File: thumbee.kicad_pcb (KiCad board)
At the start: 2 copper layers, 1 part, among them U1 msc313e

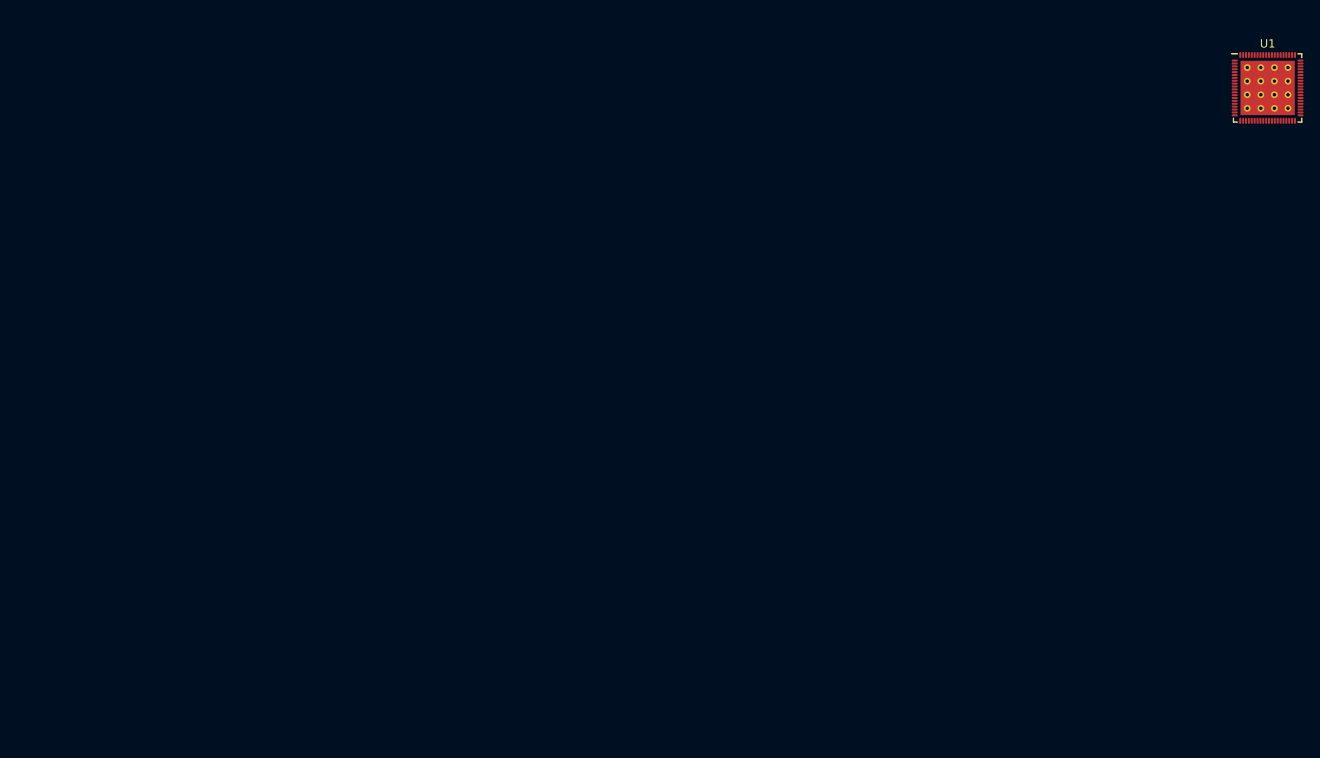
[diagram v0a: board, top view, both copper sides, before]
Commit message: Fix schematic bugs. Assign footprints.
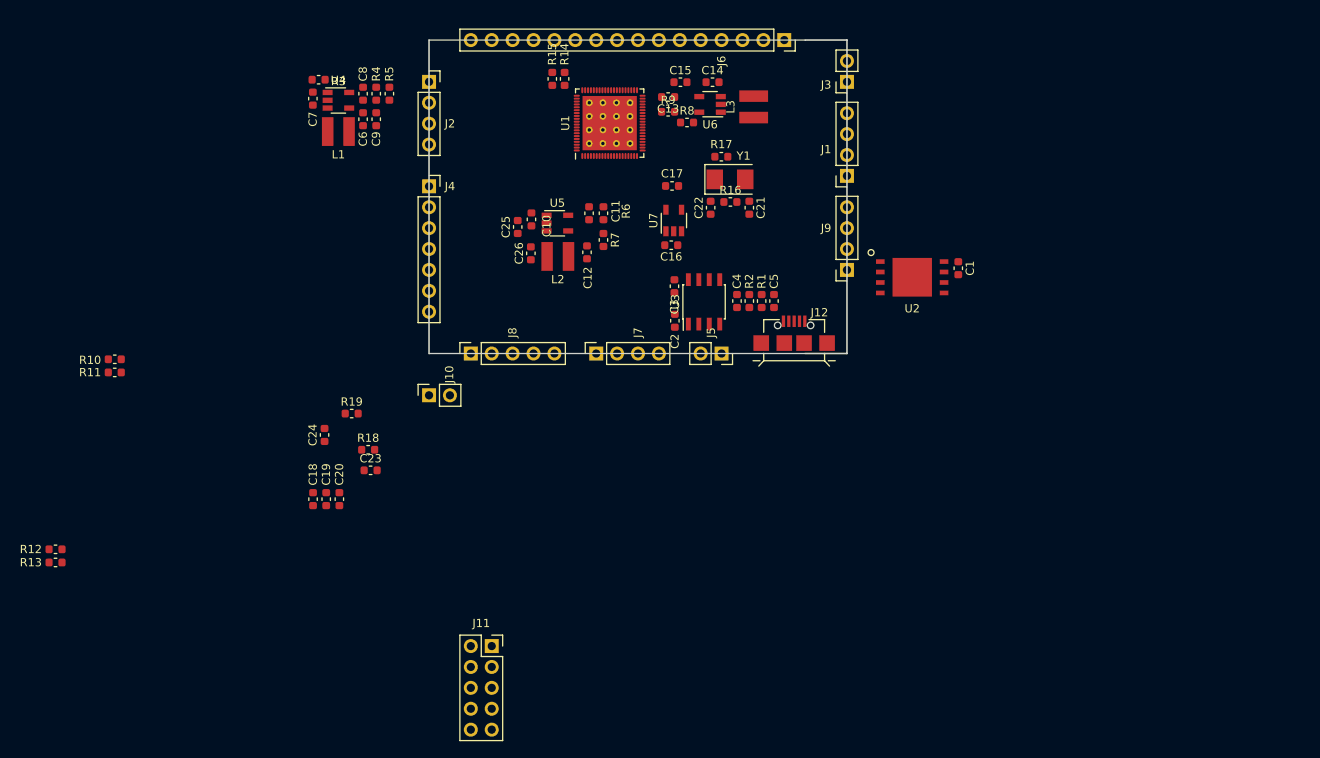
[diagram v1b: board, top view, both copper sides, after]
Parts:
- added C1: C, Capacitor_SMD:C_0603_1608Metric, F.Cu at (135.4, 109.0)
- added C10: C, Capacitor_SMD:C_0603_1608Metric, F.Cu at (83.6, 103.1)
- added C11: C, Capacitor_SMD:C_0603_1608Metric, F.Cu at (90.6, 102.3)
- added C12: C, Capacitor_SMD:C_0603_1608Metric, F.Cu at (90.3, 107.1)
- added C13: C, Capacitor_SMD:C_0603_1608Metric, F.Cu at (100.2, 88.2)
- added C14: C, Capacitor_SMD:C_0603_1608Metric, F.Cu at (105.6, 86.4)
- added C15: C, Capacitor_SMD:C_0603_1608Metric, F.Cu at (101.7, 86.4)
- added C16: C, Capacitor_SMD:C_0603_1608Metric, F.Cu at (100.6, 106.2)
- added C17: C, Capacitor_SMD:C_0603_1608Metric, F.Cu at (100.7, 99.0)
- added C18: C, Capacitor_SMD:C_0603_1608Metric, F.Cu at (57.0, 137.1)
- added C19: C, Capacitor_SMD:C_0603_1608Metric, F.Cu at (58.6, 137.1)
- added C2: C, Capacitor_SMD:C_0603_1608Metric, F.Cu at (101.0, 115.4)
- added C20: C, Capacitor_SMD:C_0603_1608Metric, F.Cu at (60.2, 137.1)
- added C21: C, Capacitor_SMD:C_0603_1608Metric, F.Cu at (110.0, 101.7)
- added C22: C, Capacitor_SMD:C_0603_1608Metric, F.Cu at (105.3, 101.7)
- added C23: C, Capacitor_SMD:C_0603_1608Metric, F.Cu at (64.0, 133.6)
- added C24: C, Capacitor_SMD:C_0603_1608Metric, F.Cu at (58.4, 129.3)
- added C25: C, Capacitor_SMD:C_0603_1608Metric, F.Cu at (81.9, 104.0)
- added C26: C, Capacitor_SMD:C_0603_1608Metric, F.Cu at (83.5, 107.2)
- added C3: C, Capacitor_SMD:C_0603_1608Metric, F.Cu at (101.0, 111.2)
- added C4: C, Capacitor_SMD:C_0603_1608Metric, F.Cu at (108.5, 113.0)
- added C5: C, Capacitor_SMD:C_0603_1608Metric, F.Cu at (113.0, 113.0)
- added C6: C, Capacitor_SMD:C_0603_1608Metric, F.Cu at (63.1, 90.9)
- added C7: C, Capacitor_SMD:C_0603_1608Metric, F.Cu at (57.0, 88.4)
- added C8: C, Capacitor_SMD:C_0603_1608Metric, F.Cu at (63.1, 87.8)
- added C9: C, Capacitor_SMD:C_0603_1608Metric, F.Cu at (64.7, 90.9)
- added J1: Conn_01x04_Male, Connector_PinSocket_2.54mm:PinSocket_1x04_P2.54mm_Vertical, F.Cu at (121.9, 97.8)
- added J10: Conn_01x02_Male, Connector_PinSocket_2.54mm:PinSocket_1x02_P2.54mm_Vertical, F.Cu at (71.1, 124.5)
- added J11: Conn_02x05_Odd_Even, Connector_PinSocket_2.54mm:PinSocket_2x05_P2.54mm_Vertical, F.Cu at (78.7, 154.9)
- added J12: USB_B, USB-MICRO-MK5P-2:USB-MICRO-B, F.Cu at (115.5, 118.1)
- added J2: Conn_01x04_Male, Connector_PinSocket_2.54mm:PinSocket_1x04_P2.54mm_Vertical, F.Cu at (71.1, 86.4)
- added J3: Conn_01x02_Male, Connector_PinSocket_2.54mm:PinSocket_1x02_P2.54mm_Vertical, F.Cu at (121.9, 86.4)
- added J4: Conn_01x07_Male, Connector_PinSocket_2.54mm:PinSocket_1x07_P2.54mm_Vertical, F.Cu at (71.1, 99.1)
- added J5: Conn_01x02_Male, Connector_PinSocket_2.54mm:PinSocket_1x02_P2.54mm_Vertical, F.Cu at (106.7, 119.4)
- added J6: Conn_01x16_Male, Connector_PinSocket_2.54mm:PinSocket_1x16_P2.54mm_Vertical, F.Cu at (114.3, 81.3)
- added J7: Conn_01x04_Male, Connector_PinSocket_2.54mm:PinSocket_1x04_P2.54mm_Vertical, F.Cu at (91.4, 119.4)
- added J8: Conn_01x05_Male, Connector_PinSocket_2.54mm:PinSocket_1x05_P2.54mm_Vertical, F.Cu at (76.2, 119.4)
- added J9: Conn_01x04_Male, Connector_PinSocket_2.54mm:PinSocket_1x04_P2.54mm_Vertical, F.Cu at (121.9, 109.2)
- added L1: L, cd32:CD32, F.Cu at (60.1, 92.4)
- added L2: L, cd32:CD32, F.Cu at (86.8, 107.6)
- added L3: L, cd32:CD32, F.Cu at (110.6, 89.4)
- added R1: R, Resistor_SMD:R_0603_1608Metric, F.Cu at (111.5, 113.0)
- added R10: R, Resistor_SMD:R_0603_1608Metric, F.Cu at (32.9, 120.1)
- added R11: R, Resistor_SMD:R_0603_1608Metric, F.Cu at (32.9, 121.7)
- added R12: R, Resistor_SMD:R_0603_1608Metric, F.Cu at (25.7, 143.2)
- added R13: R, Resistor_SMD:R_0603_1608Metric, F.Cu at (25.7, 144.8)
- added R14: R, Resistor_SMD:R_0603_1608Metric, F.Cu at (87.6, 86.0)
- added R15: R, Resistor_SMD:R_0603_1608Metric, F.Cu at (86.1, 86.0)
- added R16: R, Resistor_SMD:R_0603_1608Metric, F.Cu at (107.8, 101.0)
- added R17: R, Resistor_SMD:R_0603_1608Metric, F.Cu at (106.7, 95.5)
- added R18: R, Resistor_SMD:R_0603_1608Metric, F.Cu at (63.7, 131.1)
- added R19: 0, Resistor_SMD:R_0603_1608Metric, F.Cu at (61.7, 126.7)
- added R2: R, Resistor_SMD:R_0603_1608Metric, F.Cu at (110.0, 113.0)
- added R3: R, Resistor_SMD:R_0603_1608Metric, F.Cu at (57.7, 86.1)
- added R4: R, Resistor_SMD:R_0603_1608Metric, F.Cu at (64.7, 87.8)
- added R5: R, Resistor_SMD:R_0603_1608Metric, F.Cu at (66.3, 87.8)
- added R6: R, Resistor_SMD:R_0603_1608Metric, F.Cu at (92.3, 102.3)
- added R7: R, Resistor_SMD:R_0603_1608Metric, F.Cu at (92.3, 105.6)
- added R8: R, Resistor_SMD:R_0603_1608Metric, F.Cu at (102.5, 91.3)
- added R9: R, Resistor_SMD:R_0603_1608Metric, F.Cu at (100.2, 90.0)
- added U2: spinor, wson8-8x6mm:wson8-8x6mm, F.Cu at (129.8, 110.1)
- added U3: ht42b534-1, Package_SO:SOIC-8_3.9x4.9mm_P1.27mm, F.Cu at (104.5, 113.1)
- added U4: RT8059GJ5, Package_TO_SOT_SMD:TSOT-23-5, F.Cu at (60.1, 88.6)
- added U5: RT8059GJ5, Package_TO_SOT_SMD:TSOT-23-5, F.Cu at (86.7, 103.5)
- added U6: RT8059GJ5, Package_TO_SOT_SMD:TSOT-23-5, F.Cu at (105.3, 89.1)
- added U7: xc6204xxxxMR, Package_TO_SOT_SMD:TSOT-23-5, F.Cu at (100.9, 103.2)
- added Y1: Crystal, Crystal:Crystal_SMD_5032-2Pin_5.0x3.2mm, F.Cu at (107.7, 98.2)
- moved U1 80.1 mm to (93.1, 91.4), turned to 90 degrees
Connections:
- U1 pad 13: Net-(U1-Pad13) -> /dvdd_nodie
- U1 pad 14: Net-(U1-Pad14) -> +3.3VA
- U1 pad 17: Net-(U1-Pad17) -> /reset
- U1 pad 18: Net-(U1-Pad18) -> /console_tx
- U1 pad 19: Net-(U1-Pad19) -> /console_rx
- U1 pad 20: Net-(U1-Pad20) -> /gnd_efuse
- U1 pad 22: Net-(U1-Pad22) -> /spinor_cs
- U1 pad 23: Net-(U1-Pad23) -> /spinor_miso
- U1 pad 24: Net-(U1-Pad24) -> /spinor_wp
- U1 pad 25: Net-(U1-Pad25) -> /spinor_mosi
- U1 pad 26: Net-(U1-Pad26) -> /spinor_sck
- U1 pad 27: Net-(U1-Pad27) -> +3.3VA
- U1 pad 28: Net-(U1-Pad28) -> /xtal_in
- U1 pad 29: Net-(U1-Pad29) -> /xtal_out
- U1 pad 3: Net-(U1-Pad3) -> +1V8
- U1 pad 30: Net-(U1-Pad30) -> +3.3VA
- U1 pad 35: Net-(U1-Pad35) -> /vddp1
- U1 pad 4: Net-(U1-Pad4) -> +1V8
- U1 pad 40: Net-(U1-Pad40) -> +1V0
- U1 pad 43: Net-(U1-Pad43) -> /vddp2
- U1 pad 5: Net-(U1-Pad5) -> +1V0
- U1 pad 6: Net-(U1-Pad6) -> +1V8
- U1 pad 60: Net-(U1-Pad60) -> +1V0
- U1 pad 61: Net-(U1-Pad61) -> +1V0
- U1 pad 62: Net-(U1-Pad62) -> /vddp3
- U1 pad 67: Net-(U1-Pad67) -> +1V0
- U1 pad 7: Net-(U1-Pad7) -> +3.3VA
- U1 pad 74: Net-(U1-Pad74) -> +3.3VA
- U1 pad 77: Net-(U1-Pad77) -> +3.3VA
- U1 pad 8: Net-(U1-Pad8) -> +1V0
- U1 pad 81: Net-(U1-Pad81) -> GND
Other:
- board outline added: 50.8 x 38.1 mm
- net class Default: clearance 0.2 -> 0.15; trace_width 0.25 -> 0.15
- rule trace_clearance: 0.2 -> 0.15
- rule trace_min: 0.2 -> 0.15

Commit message: QFN footprint fix up. Replace headers with a module footprint. Very rought parts layout and some routing.
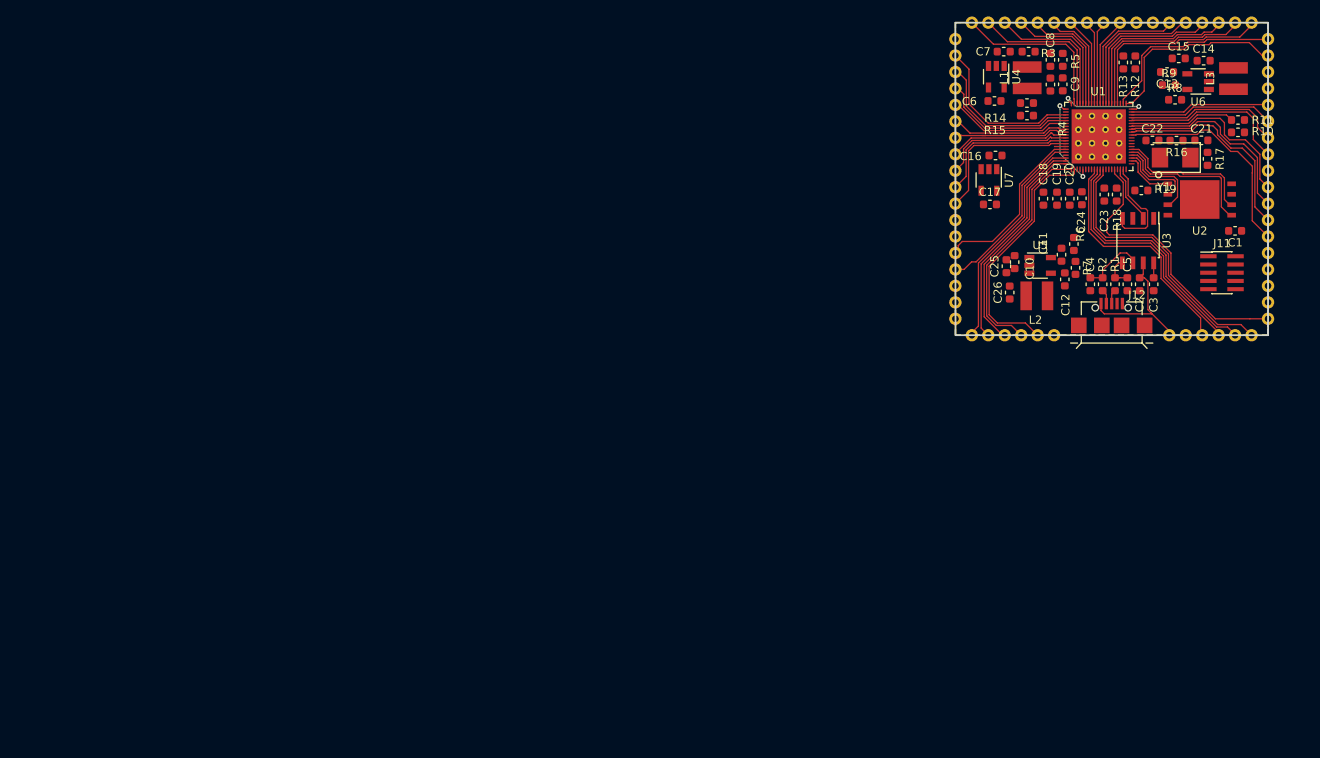
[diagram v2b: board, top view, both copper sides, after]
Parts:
- removed J1, J2, J7, J9: Conn_01x04_Male, Connector_PinSocket_2.54mm:PinSocket_1x04_P2.54mm_Vertical
- removed J10, J3, J5: Conn_01x02_Male, Connector_PinSocket_2.54mm:PinSocket_1x02_P2.54mm_Vertical
- removed J4: Conn_01x07_Male, Connector_PinSocket_2.54mm:PinSocket_1x07_P2.54mm_Vertical
- removed J6: Conn_01x16_Male, Connector_PinSocket_2.54mm:PinSocket_1x16_P2.54mm_Vertical
- removed J8: Conn_01x05_Male, Connector_PinSocket_2.54mm:PinSocket_1x05_P2.54mm_Vertical
- added MOD1: thumbee, thumbee:thumbee, F.Cu at (154.1, 98.2)
- J11: footprint Connector_PinSocket_2.54mm:PinSocket_2x05_P2.54mm_Vertical -> Connector_PinHeader_1.00mm:PinHeader_2x05_P1.00mm_Vertical_SMD
- moved R12 144.0 mm to (157.0, 84.0), turned to 270 degrees
- moved R13 143.3 mm to (155.5, 84.0), turned to 270 degrees
- moved R11 139.9 mm to (169.4, 91.0), turned to 180 degrees
- moved R10 139.3 mm to (169.4, 92.5), turned to 180 degrees
- moved R19 99.7 mm to (157.7, 99.6)
- moved J11 99.7 mm to (167.5, 109.6)
- moved C24 96.4 mm to (150.5, 100.5)
- moved R18 96.1 mm to (154.7, 100.1), turned to 270 degrees
- moved C19 96.0 mm to (147.4, 100.6)
- moved C18 96.0 mm to (145.8, 100.6)
- moved C20 96.0 mm to (149.0, 100.6)
- moved C23 95.3 mm to (153.2, 100.1), turned to 90 degrees
- moved R3 86.4 mm to (144.0, 82.7)
- moved C7 84.2 mm to (141.0, 82.7), turned to 180 degrees
- moved L1 84.0 mm to (143.8, 85.9), turned to 270 degrees
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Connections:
- U1 pad 1: Net-(J8-Pad5) -> /aud_miccm0
- U1 pad 10: Net-(J7-Pad2) -> /sar_gpio2
- U1 pad 11: Net-(J7-Pad3) -> /sar_gpio1
- U1 pad 12: Net-(J7-Pad4) -> /sar_gpio0
- U1 pad 15: Net-(J4-Pad7) -> /pm_sd_cdz
- U1 pad 16: Net-(J5-Pad2) -> /pm_irin
- U1 pad 2: Net-(J8-Pad1) -> /aud_lineout_l0
- U1 pad 31: Net-(J9-Pad1) -> /eth_rn
- U1 pad 32: Net-(J9-Pad2) -> /eth_rp
- U1 pad 33: Net-(J9-Pad3) -> /eth_tn
- U1 pad 34: Net-(J9-Pad4) -> /eth_tp
- U1 pad 36: Net-(J1-Pad1) -> /fuart_rx
- U1 pad 37: Net-(J1-Pad2) -> /fuart_tx
- U1 pad 38: Net-(J1-Pad3) -> /fuart_cts
- U1 pad 39: Net-(J1-Pad4) -> /fuart_rtx
- U1 pad 41: Net-(J3-Pad1) -> /i2c1_scl
- U1 pad 42: Net-(J3-Pad2) -> /i2c1_sda
- U1 pad 44: Net-(J6-Pad1) -> /sr_io2
- U1 pad 45: Net-(J6-Pad2) -> /sr_io3
- U1 pad 46: Net-(J6-Pad3) -> /sr_io4
- U1 pad 47: Net-(J6-Pad4) -> /sr_io5
- U1 pad 48: Net-(J6-Pad5) -> /sr_io6
- U1 pad 49: Net-(J6-Pad6) -> /sr_io7
- U1 pad 50: Net-(J6-Pad7) -> /sr_io8
- U1 pad 51: Net-(J6-Pad8) -> /sr_io9
- U1 pad 52: Net-(J6-Pad9) -> /sr_io10
- U1 pad 53: Net-(J6-Pad10) -> /sr_io11
- U1 pad 54: Net-(J6-Pad11) -> /sr_io12
- U1 pad 55: Net-(J6-Pad12) -> /sr_io13
- U1 pad 56: Net-(J6-Pad13) -> /sr_io14
- U1 pad 57: Net-(J6-Pad14) -> /sr_io15
- U1 pad 58: Net-(J6-Pad15) -> /sr_io16
- U1 pad 59: Net-(J6-Pad16) -> /sr_io17
- U1 pad 63: Net-(J2-Pad1) -> /spi0_cz
- U1 pad 64: Net-(J2-Pad2) -> /spi0_ck
- U1 pad 65: Net-(J2-Pad3) -> /spi0_di
- U1 pad 66: Net-(J2-Pad4) -> /spi0_do
- U1 pad 68: Net-(J4-Pad1) -> /sd_clk
- U1 pad 69: Net-(J4-Pad2) -> /sd_cmd
- U1 pad 70: Net-(J4-Pad3) -> /sd_d0
- U1 pad 71: Net-(J4-Pad4) -> /sd_d1
- U1 pad 72: Net-(J4-Pad5) -> /sd_d2
- U1 pad 73: Net-(J4-Pad6) -> /sd_d3
- U1 pad 75: Net-(J10-Pad1) -> /usb_dm
- U1 pad 76: Net-(J10-Pad2) -> /usb_dp
- U1 pad 78: Net-(J8-Pad2) -> /aud_vag
- U1 pad 79: Net-(J8-Pad3) -> /aud_vrm_adc
- U1 pad 80: Net-(J8-Pad4) -> /aud_micin0
- U1 pad 9: Net-(J7-Pad1) -> /sar_gpio3
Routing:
- net /pm_irin: track 0.00 -> 34.1 mm
- net /sar_gpio0: track 0.00 -> 32.8 mm
- net /sar_gpio1: track 0.00 -> 31.2 mm
- net /aud_lineout_l0: track 0.00 -> 30.1 mm
- net /sar_gpio2: track 0.00 -> 29.8 mm
- net /sar_gpio3: track 0.00 -> 29.1 mm
- net /aud_miccm0: track 0.00 -> 28.2 mm
- net /aud_vag: track 0.00 -> 26.9 mm
- net /aud_micin0: track 0.00 -> 26.5 mm
- net /aud_vrm_adc: track 0.00 -> 26.2 mm
- net /eth_rn: track 0.00 -> 25.6 mm
- net /eth_rp: track 0.00 -> 24.9 mm
- net /sr_io2: track 0.00 -> 24.1 mm
- net /eth_tn: track 0.00 -> 23.6 mm
- net /i2c1_scl: track 0.00 -> 23.0 mm
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- added copper zone on B.Cu, net GND
- added copper zone on F.Cu, net GND
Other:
- board size 50.8 x 38.1 mm -> 38 x 38 mm

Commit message: Rough all routed.
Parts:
- added C27: C, Capacitor_SMD:C_0603_1608Metric, F.Cu at (158.7, 89.3)
- J11: moved to B.Cu
- moved C26 10.8 mm to (152.2, 109.4)
- moved R9 10.3 mm to (171.3, 87.4), turned to 270 degrees
- moved R8 9.42 mm to (170.6, 85.1)
- moved C25 9.42 mm to (150.7, 109.4)
- moved U2 8.21 mm to (167.5, 108.4), turned to 90 degrees
- moved L2 7.86 mm to (147.8, 105.0), turned to 180 degrees
- moved C17 7.37 mm to (144.0, 95.6), turned to 270 degrees
- moved C4 6.85 mm to (158.3, 111.0)
- moved R7 6.24 mm to (143.9, 111.3), turned to 180 degrees
- moved R17 6.10 mm to (159.7, 95.7), turned to 270 degrees
- moved C22 6.00 mm to (165.1, 93.3), turned to 270 degrees
- moved C12 5.92 mm to (144.7, 105.8), turned to 270 degrees
- moved C21 5.89 mm to (165.1, 99.4), turned to 270 degrees
- moved R6 5.85 mm to (146.9, 111.3), turned to 180 degrees
- moved C11 5.59 mm to (146.9, 112.9), turned to 180 degrees
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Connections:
- J11 pad 3: /spinor_mosi -> /spinor_hold
- J11 pad 4: /spinor_wp -> /spinor_miso
- J11 pad 5: /spinor_miso -> /spinor_sck
- J11 pad 6: Net-(J11-Pad6) -> /spinor_wp
- J11 pad 7: /spinor_sck -> /spinor_mosi
- J11 pad 9: /spinor_hold -> Net-(J11-Pad9)
- MOD1 pad 34: Net-(MOD1-Pad34) -> GND
- MOD1 pad 35: Net-(MOD1-Pad35) -> GND
- MOD1 pad 36: Net-(MOD1-Pad36) -> GND
- MOD1 pad 50: Net-(MOD1-Pad50) -> /pm_gpio4
- MOD1 pad 51: Net-(MOD1-Pad51) -> GND
- MOD1 pad 52: Net-(MOD1-Pad52) -> GND
- MOD1 pad 53: Net-(MOD1-Pad53) -> GND
- MOD1 pad 58: Net-(MOD1-Pad58) -> GND
- U1 pad 21: Net-(U1-Pad21) -> /pm_gpio4
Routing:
- net GND: track 0.00 -> 315.8 mm, vias 0 -> 36
- net +1V8: track 0.00 -> 131.3 mm, vias 0 -> 7
- net +5V: track 17.7 -> 102.6 mm, vias 0 -> 7
- net +3V3: track 0.00 -> 83.6 mm, vias 0 -> 8
- net +3.3VA: track 1.39 -> 46.8 mm, vias 0 -> 7
- net /reset: track 0.00 -> 34.7 mm, vias 0 -> 1
- net /pm_gpio4: track 0.00 -> 30.1 mm
- net /pm_sd_cdz: track 0.00 -> 24.2 mm, vias 0 -> 2
- net +1V0: track 22.3 -> 45.8 mm, vias 4 -> 5
- net /spinor_cs: track 6.21 -> 25.9 mm, vias 0 -> 1
- net /spinor_miso: track 9.46 -> 27.6 mm, vias 0 -> 1
- net /spinor_wp: track 11.1 -> 29.1 mm, vias 0 -> 1
- net Net-(C14-Pad2): track 0.00 -> 12.9 mm
- net /xtal_out: track 0.00 -> 10.4 mm
- net Net-(C21-Pad1): track 0.00 -> 8.82 mm
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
